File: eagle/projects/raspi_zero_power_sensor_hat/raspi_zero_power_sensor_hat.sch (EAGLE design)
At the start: 71 parts, among them J1 JST-PH-2TH-RA, J2 USB_MICROB_RECPT, J3 HEADER-1x2-2.54MM, J4 MOL-KK-2-V, J5 RECEPTACLE-2x7-2.54MM, J6 MOL-KK-4-RA, J7 MOL-KK-3P-V, Q1 PMOS-ENHANCE-8A, Q2 PMOS-ENHANCE-8A, U1 BUFFER-1-SCHMITT, U2 TPS61089RNRR, U3 INA219AIDCNR, U4 MCP73831T, U5 MS560702BA03-50, U6 PCT2075D,118, U7 SSCMNNN015PA2A3, U8 MAX11613EUA+, U9 BUFFER-1-SCHMITT

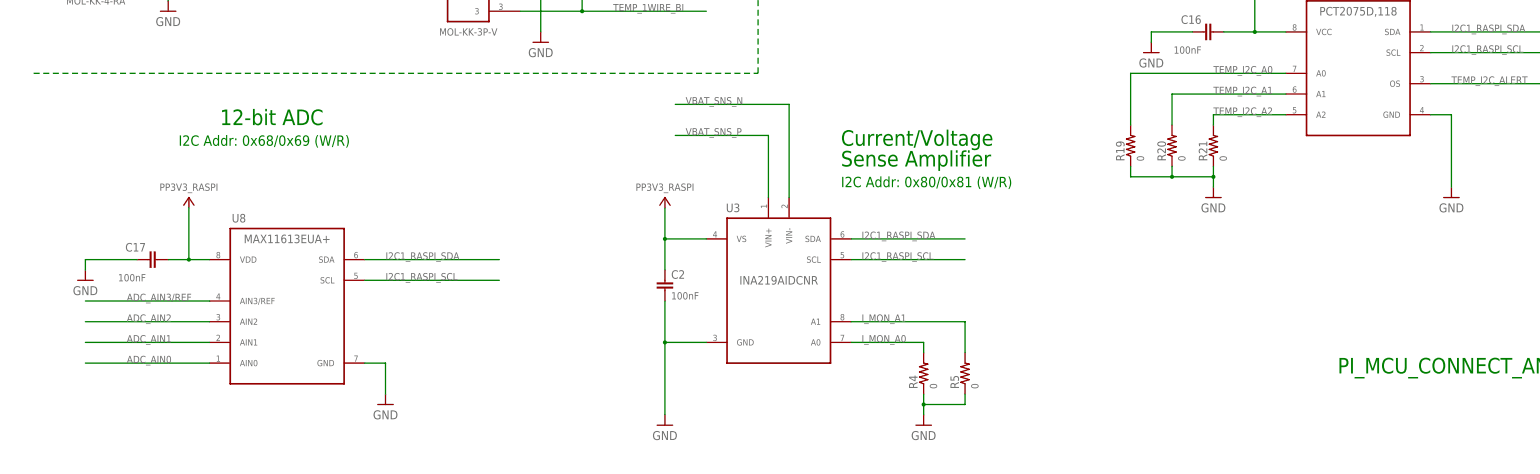
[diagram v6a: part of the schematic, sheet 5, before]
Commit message: added mounting for for Raspi
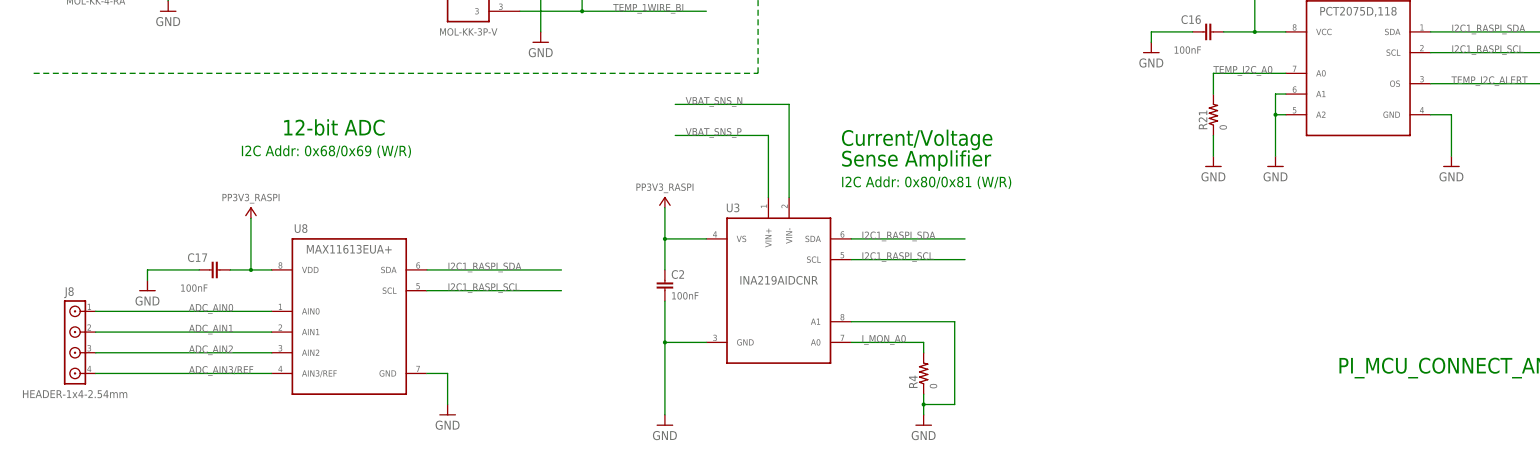
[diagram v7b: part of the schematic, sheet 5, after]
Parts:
- removed R19, R20, R26, R5: 0, daqcs:RES_0R0_0603
- removed U9: BUFFER-1-SCHMITT, daqcs:BUFFER-1-SCHMITT_BUF1_TSSOP5
- added J8: HEADER-1x4-2.54mm, daqcs:HEADER-1X4-254MM_1X4_254MM_TH
- C19: value 100nF -> 10uF; device daqcs:CAP_100NF0_0603 -> daqcs:CAP_10UF0_0603
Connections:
- removed net I_MON_A1: R5.2, U3.A1
- removed net TEMP_I2C_A1: R20.2, U6.A1
- removed net TEMP_I2C_A2: R21.2, U6.A2
- removed net USB_BUFFER_OUT: R27.1, U9.Y
- removed net VBAT_LOAD_DISABLE: R26.1, U9.A
- net ADC_AIN0: now also J8.1
- net ADC_AIN1: now also J8.2
- net ADC_AIN2: now also J8.3
- net ADC_AIN3/REF: now also J8.4
- net GND: now also C19.2, U3.A1, U6.A1, U6.A2; no longer C19.1, R19.1, R20.1, R5.1, U9.GND
- net PP5V0_USB: now also R27.1; no longer C19.2, R26.2, U9.VCC
- net TEMP_I2C_A0: now also R21.2; no longer R19.2
- net VBAT: now also C19.1
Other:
- note added: "MSP430 I/O is 3.3V logic"
- note added: "Vin UVLO: 2.5V (MAX)"
- note added: "Vt+: 2.79V (MAX)"
- note added: "Vt-: 1.58V (MIN)"
- moved on the sheet: C17, C19, R21, R27, U8

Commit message: messed around with layout
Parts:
- added H1, H2, H3, H4: MOUNT-HOLE_2.75, daqcs:MOUNT-HOLE_2.75
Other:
- note removed: "MOUNT_TP_CONFIG"
